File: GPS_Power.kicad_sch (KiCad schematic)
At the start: 11 parts, among them J7 U.FL-R-SMT-1, U10 BTS5090-1EJA, U14 ADM1176-1ARMZ-R7, U8 S1216V8

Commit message: temp
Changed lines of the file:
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@@
 		)
 	)
-	(hierarchical_label "SDA_BUS"
+	(hierarchical_label "SDA"
 		(shape bidirectional)
 		(at 215.9 62.23 0)
+		(fields_autoplaced yes)
+		(effects
+			(font
+				(size 1.27 1.27)
+			)
+			(justify left)
+		)
+	)
+	(hierarchical_label "SCL"
+		(shape bidirectional)
+		(at 215.9 59.69 0)
 		(fields_autoplaced yes)
 		(effects
@@
 		)
 	)
-	(hierarchical_label "SCL_BUS"
-		(shape bidirectional)
-		(at 215.9 59.69 0)
-		(fields_autoplaced yes)
-		(effects
-			(font
-				(size 1.27 1.27)
-			)
-			(justify left)
-		)
-	)

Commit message: v1 done
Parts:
- U14: symbol Mainboard:ADM1176-1ARMZ-R7 -> Argus-IC:ADM1176-1ARMZ-R7
- U8: symbol MainBoard:S1216V8 -> Argus-Miscellaneous:S1216V8
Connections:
- no-connect marks 17 -> 18
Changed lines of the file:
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@@
+	)
+	(no_connect
+		(at 78.74 53.34)
 	)
 	(no_connect
@@
 	)
 	(symbol
-		(lib_id "Mainboard:ADM1176-1ARMZ-R7")
+		(lib_id "Argus-IC:ADM1176-1ARMZ-R7")
 		(at 148.59 59.69 0)
 		(unit 1)
@@
 	)
 	(symbol
-		(lib_id "MainBoard:S1216V8")
+		(lib_id "Argus-Miscellaneous:S1216V8")
 		(at 121.92 113.03 0)
 		(unit 1)

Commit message: Updated i2c device addresses and mcu caps
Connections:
- net GND: now also U14.8 (A0), U14.9 (A1)
- no-connect marks 18 -> 16
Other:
- note added: "0x40"
- note removed: "0x4A"
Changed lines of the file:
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@@
+	)
+	(junction
+		(at 132.08 57.15)
+		(diameter 0)
+		(color 0 0 0 0)
 	)
 	(junction
@@
 	)
 	(no_connect
-		(at 132.08 59.69)
-	)
-	(no_connect
 		(at 139.7 120.65)
 	)
@@
 	)
 	(no_connect
-		(at 132.08 57.15)
-	)
-	(no_connect
 		(at 104.14 100.33)
 	)
@@
 	(wire
 		(pts
+			(xy 130.81 57.15) (xy 130.81 67.31)
+		)
+		(stroke
+			(width 0)
+			(type default)
+		)
+	)
+	(wire
+		(pts
 			(xy 67.31 120.65) (xy 92.71 120.65)
 		)
@@
 	(wire
 		(pts
+			(xy 132.08 57.15) (xy 130.81 57.15)
+		)
+		(stroke
+			(width 0)
+			(type default)
+		)
+	)
+	(wire
+		(pts
 			(xy 121.92 64.77) (xy 132.08 64.77)
 		)
@@
 		)
 	)
-	(text "0x4A"
+	(wire
+		(pts
+			(xy 132.08 57.15) (xy 132.08 59.69)
+		)
+		(stroke
+			(width 0)
+			(type default)
+		)
+	)
+	(text "0x40"
 		(exclude_from_sim no)
 		(at 168.148 83.058 0)
@@
 		)
 	)
+	(symbol
+		(lib_id "power:GND")
+		(at 130.81 67.31 0)
+		(unit 1)
+		(exclude_from_sim no)
+		(in_bom yes)
+		(on_board yes)
+		(dnp no)
+		(property "Reference" "#PWR0115"
+			(at 130.81 73.66 0)
+			(effects
+				(font
+					(size 1.27 1.27)
+				)
+				(hide yes)
+			)
+		)
+		(property "Value" "GND"
+			(at 130.81 71.12 0)
+			(effects
+				(font
+					(size 1.27 1.27)
+				)
+			)
+		)
+		(property "Footprint" ""
+			(at 130.81 67.31 0)
+			(effects
+				(font
+					(size 1.27 1.27)
+				)
+				(hide yes)
+			)
+		)
+		(property "Datasheet" ""
+			(at 130.81 67.31 0)
+			(effects
+				(font
+					(size 1.27 1.27)
+				)
+				(hide yes)
+			)
+		)
+		(property "Description" "Power symbol creates a global label with name \"GND\" , ground"
+			(at 130.81 67.31 0)
+			(effects
+				(font
+					(size 1.27 1.27)
+				)
+				(hide yes)
+			)
+		)
+		(pin "1"
+		)
+		(instances
+			(project "Avionics-MainBoard"
+				(path "/4c932743-8c6f-426e-9c1f-5a3f2b32c70d/1ff82478-f00f-4d48-a429-2ed9117c0498"
+					(reference "#PWR0115")
+					(unit 1)
+				)
+			)
+		)
+	)

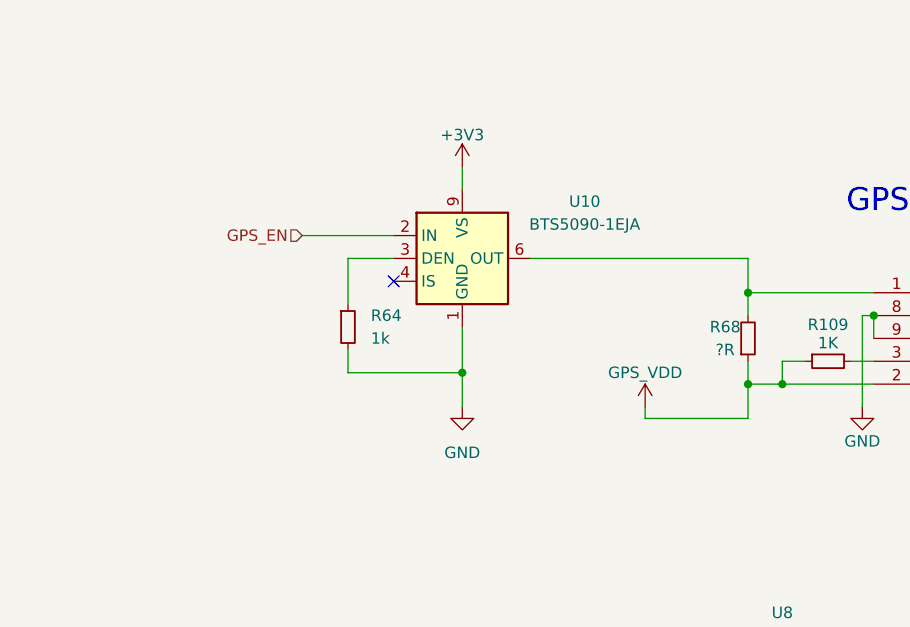
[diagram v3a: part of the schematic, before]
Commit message: Fixed schematic bugs and corresponding layout modifications
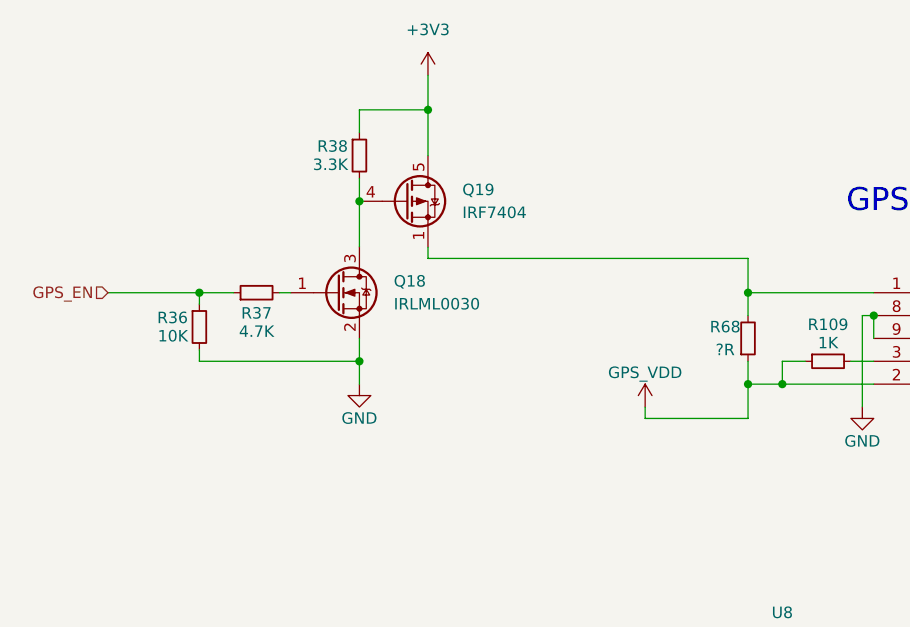
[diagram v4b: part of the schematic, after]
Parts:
- removed R64: 1k, Resistor_SMD:R_0603_1608Metric, symbol Device:R_Small
- removed U10: BTS5090-1EJA, Package_SO:Infineon_PG-DSO-8-43, symbol Power_Management:BTS5090-1EJA
- added Q18: IRLML0030, Package_TO_SOT_SMD:SOT-23, symbol Transistor_FET:IRLML0030
- added Q19: IRF7404, Package_SO:SOIC-8_3.9x4.9mm_P1.27mm, symbol Transistor_FET:IRF7404
- added R36: 10K, Resistor_SMD:R_0603_1608Metric, symbol Device:R_Small
- added R37: 4.7K, Resistor_SMD:R_0603_1608Metric, symbol Device:R_Small
- added R38: 3.3K, Resistor_SMD:R_0603_1608Metric, symbol Device:R_Small
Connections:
- net +3V3: now also Q19.5 (D), Q19.6 (D), Q19.7 (D), Q19.8 (D), R38.1
- net GND: now also Q18.2 (S), R36.2
- net GPS_EN: now also R36.1, R37.1
- net at R68.2, U14.1 (VCC): now also Q19.1 (S), Q19.2 (S), Q19.3 (S)
- new net: Q18.3 (D), Q19.4 (G), R38.2
- new net: Q18.1 (G), R37.2
- no-connect marks 16 -> 15

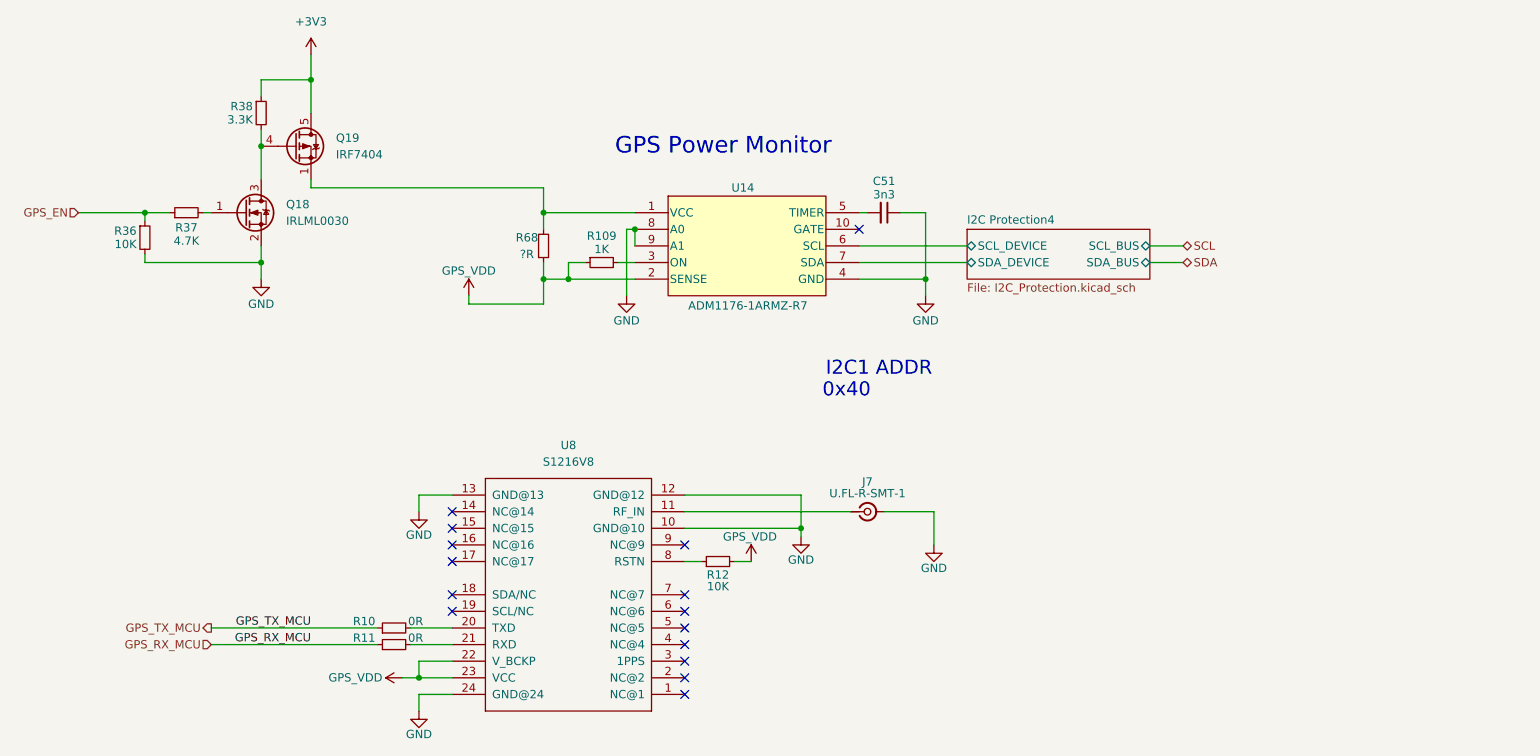
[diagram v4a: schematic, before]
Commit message: Added better protection to SD card, Jetson IO, and added address breakouts to power monitors
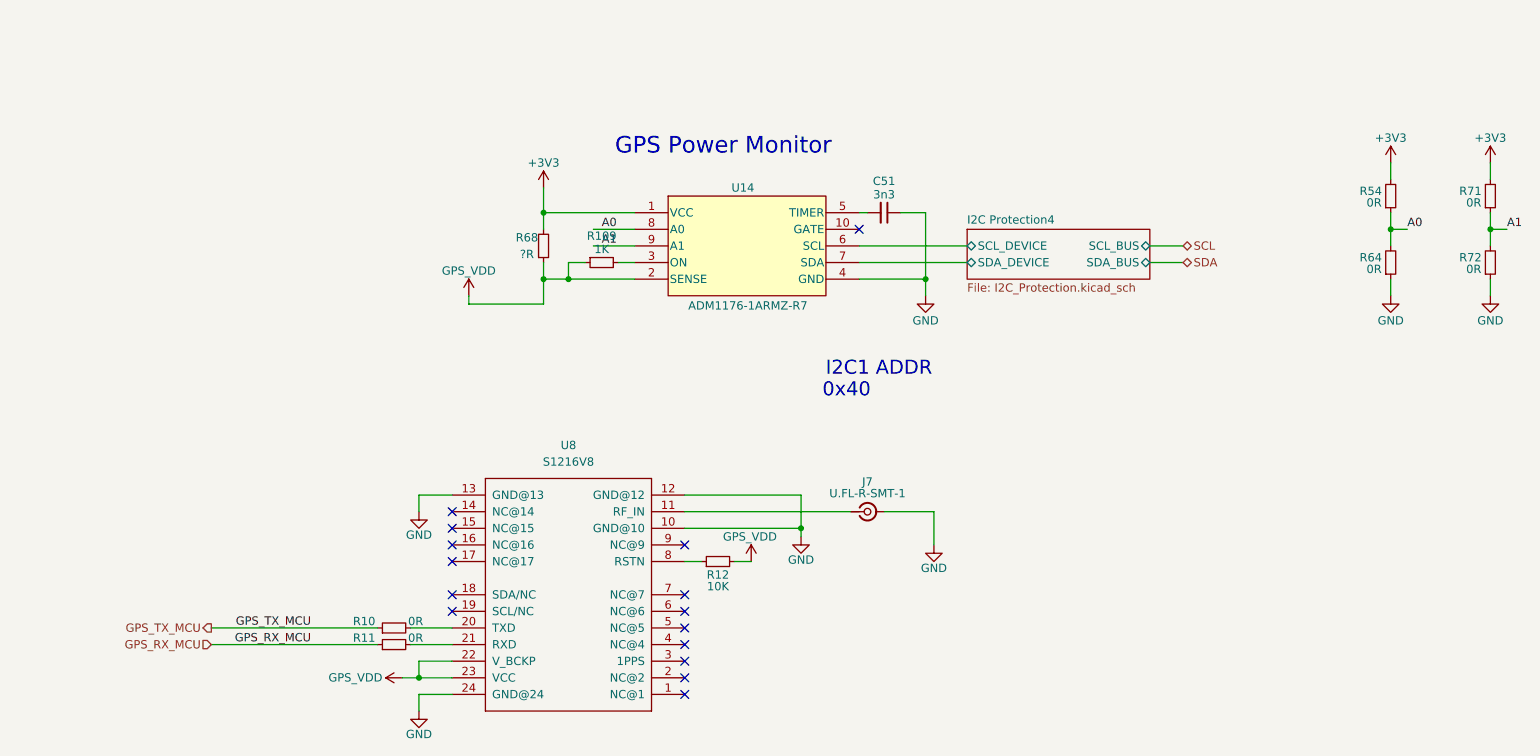
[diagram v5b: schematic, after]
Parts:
- removed Q18: IRLML0030, Package_TO_SOT_SMD:SOT-23, symbol Transistor_FET:IRLML0030
- removed Q19: IRF7404, Package_SO:SOIC-8_3.9x4.9mm_P1.27mm, symbol Transistor_FET:IRF7404
- removed R36: 10K, Resistor_SMD:R_0603_1608Metric, symbol Device:R_Small
- removed R37: 4.7K, Resistor_SMD:R_0603_1608Metric, symbol Device:R_Small
- removed R38: 3.3K, Resistor_SMD:R_0603_1608Metric, symbol Device:R_Small
- added R54, R64, R71, R72: 0R, Resistor_SMD:R_0603_1608Metric, symbol Device:R_Small
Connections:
- net +3V3: now also R68.2, U14.1 (VCC), R54.2, R71.2
- net GND: now also R64.1, R72.1; no longer U14.8 (A0), U14.9 (A1)
- new net A0: R54.1, R64.2, U14.8 (A0)
- new net A1: R71.1, R72.2, U14.9 (A1)

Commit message: Updated version to v2.1
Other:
- company: (none) -> Carnegie Mellon University
- title: (none) -> Argus Mainboard
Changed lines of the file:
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@@
 	(generator_version "8.0")
 	(paper "A4")
+	(title_block
+		(title "Argus Mainboard")
+		(date "2024-11-19")
+		(rev "v2.1")
+		(company "Carnegie Mellon University")
+		(comment 1 "M. Holliday")
+		(comment 2 "N. Khera")
+		(comment 3 "V. Rajesh")
+	)
 	(junction
 		(at 247.65 57.15)
